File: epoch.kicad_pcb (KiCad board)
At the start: 4 copper layers, 28 x 34 mm, 29 parts, among them J1 USB_OTG, J2 CONN_01X05, P3 CONN_01X10, SW1 SW_Reset, SW2 SW_Up, SW3 SW_Middle, SW4 SW_Down, U1 MIC5219-3.3BM5, U2 ATSAMD21Ennc-AU, U3 DS3231MZ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

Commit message: Add back corner drill holes
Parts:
- added REF**: 1pin, Connectors:1pin_nosilk, F.Cu at (103.3, 56.5)
- added REF**: 1pin, Connectors:1pin_nosilk, F.Cu at (127.3, 56.5)
- added REF**: 1pin, Connectors:1pin_nosilk, F.Cu at (103.4, 86.4)
- added REF**: 1pin, Connectors:1pin_nosilk, F.Cu at (127.3, 86.4)
- renumbered D1 to LED
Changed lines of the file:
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@@
     (links 80)
     (no_connects 0)
-    (area 101.218844 54.355999 129.463801 88.620601)
+    (area 82.8926 44.9831 152.154639 97.2934)
     (thickness 1.6002)
     (drawings 20)
@@
     (1 In1.Cu signal)
     (2 In2.Cu signal)
-    (31 B.Cu signal hide)
+    (31 B.Cu signal)
     (34 B.Paste user)
     (35 F.Paste user)
@@
   )
   (setup
-    (last_trace_width 0.3)
+    (last_trace_width 0.1524)
     (user_trace_width 0.1524)
     (user_trace_width 0.2)
@@
       (effects (font (size 1 1) (thickness 0.15)))
     )
-    (fp_text user %R (at -4.1275 -13.1445 180) (layer F.Fab)
+    (fp_text user %R (at -18.3515 -15.24 180) (layer F.Fab)
       (effects (font (size 1 1) (thickness 0.15)))
     )
@@
       (net 2 "(GND)"))
   )
+  (module Connectors:1pin_nosilk (layer F.Cu)
+    (at 103.3272 56.4642)
+    (descr "module 1 pin (ou trou mecanique de percage)")
+    (tags DEV)
+    (fp_text reference REF** (at -9.271 -3.302) (layer F.SilkS)
+      (effects (font (size 1 1) (thickness 0.15)))
+    )
+    (fp_text value 1pin (at -8.5725 -0.381) (layer F.Fab) hide
+      (effects (font (size 1 1) (thickness 0.15)))
+    )
+    (fp_circle (center 0 0) (end 2 0.8) (layer F.Fab) (width 0.1))
+    (fp_circle (center 0 0) (end 2.6 0) (layer F.CrtYd) (width 0.05))
+    (pad "" np_thru_hole circle (at 0 0) (size 2.2 2.2) (drill 2.2) (layers *.Cu *.Mask))
+  )
+  (module Connectors:1pin_nosilk (layer F.Cu)
+    (at 127.3048 56.5404)
+    (descr "module 1 pin (ou trou mecanique de percage)")
+    (tags DEV)
+    (fp_text reference REF** (at 1.2192 -13.2334) (layer F.SilkS)
+      (effects (font (size 1 1) (thickness 0.15)))
+    )
+    (fp_text value 1pin (at -20.7518 -11.2014) (layer F.Fab) hide
+      (effects (font (size 1 1) (thickness 0.15)))
+    )
+    (fp_circle (center 0 0) (end 2 0.8) (layer F.Fab) (width 0.1))
+    (fp_circle (center 0 0) (end 2.6 0) (layer F.CrtYd) (width 0.05))
+    (pad "" np_thru_hole circle (at 0 0) (size 2.2 2.2) (drill 2.2) (layers *.Cu *.Mask))
+  )
+  (module Connectors:1pin_nosilk (layer F.Cu)
+    (at 103.4288 86.4108)
+    (descr "module 1 pin (ou trou mecanique de percage)")
+    (tags DEV)
+    (fp_text reference REF** (at -9.271 -3.302) (layer F.SilkS)
+      (effects (font (size 1 1) (thickness 0.15)))
+    )
+    (fp_text value 1pin (at -8.5725 -0.381) (layer F.Fab) hide
+      (effects (font (size 1 1) (thickness 0.15)))
+    )
+    (fp_circle (center 0 0) (end 2 0.8) (layer F.Fab) (width 0.1))
+    (fp_circle (center 0 0) (end 2.6 0) (layer F.CrtYd) (width 0.05))
+    (pad "" np_thru_hole circle (at 0 0) (size 2.2 2.2) (drill 2.2) (layers *.Cu *.Mask))
+  )
+  (module Connectors:1pin_nosilk (layer F.Cu)
+    (at 127.2794 86.4108)
+    (descr "module 1 pin (ou trou mecanique de percage)")
+    (tags DEV)
+    (fp_text reference REF** (at -9.271 -3.302) (layer F.SilkS)
+      (effects (font (size 1 1) (thickness 0.15)))
+    )
+    (fp_text value 1pin (at 19.4056 1.8542) (layer F.Fab) hide
+      (effects (font (size 1 1) (thickness 0.15)))
+    )
+    (fp_circle (center 0 0) (end 2 0.8) (layer F.Fab) (width 0.1))
+    (fp_circle (center 0 0) (end 2.6 0) (layer F.CrtYd) (width 0.05))
+    (pad "" np_thru_hole circle (at 0 0) (size 2.2 2.2) (drill 2.2) (layers *.Cu *.Mask))
+  )
   (module Buttons_Switches_SMD:SW_SPST_B3U-3000P (layer B.Cu)
     (at 102.616 61.468 270)
@@
     (tags "LED led 0805 SMD smd SMT smt smdled SMDLED smtled SMTLED")
     (attr smd)
-    (fp_text reference D1 (at 0 -1.45 90) (layer F.SilkS)
-      (effects (font (size 1 1) (thickness 0.15)))
-    )
-    (fp_text value LED (at -0.4318 9.3472 90) (layer F.Fab)
+    (fp_text reference LED (at -0.7112 -1.524 90) (layer F.SilkS)
+      (effects (font (size 1 1) (thickness 0.15)))
+    )
+    (fp_text value LED (at -0.8382 11.303 90) (layer F.Fab)
       (effects (font (size 1 1) (thickness 0.15)))
     )
@@
   (gr_line (start 111.0615 88.483) (end 111.887 87.63) (angle 90) (layer Edge.Cuts) (width 0.254))
   (gr_line (start 103.4034 88.4936) (end 111.0488 88.4936) (angle 90) (layer Edge.Cuts) (width 0.254))
-  (gr_text 3.3V (at 126.492 86.614) (layer F.SilkS)
+  (gr_text 3.3V (at 121.158 86.741) (layer F.SilkS)
     (effects (font (size 0.6 0.6) (thickness 0.125)))
   )
-  (gr_text SDIO (at 126.365 85.344) (layer F.SilkS)
+  (gr_text SDIO (at 121.285 85.471) (layer F.SilkS)
     (effects (font (size 0.6 0.6) (thickness 0.125)))
   )

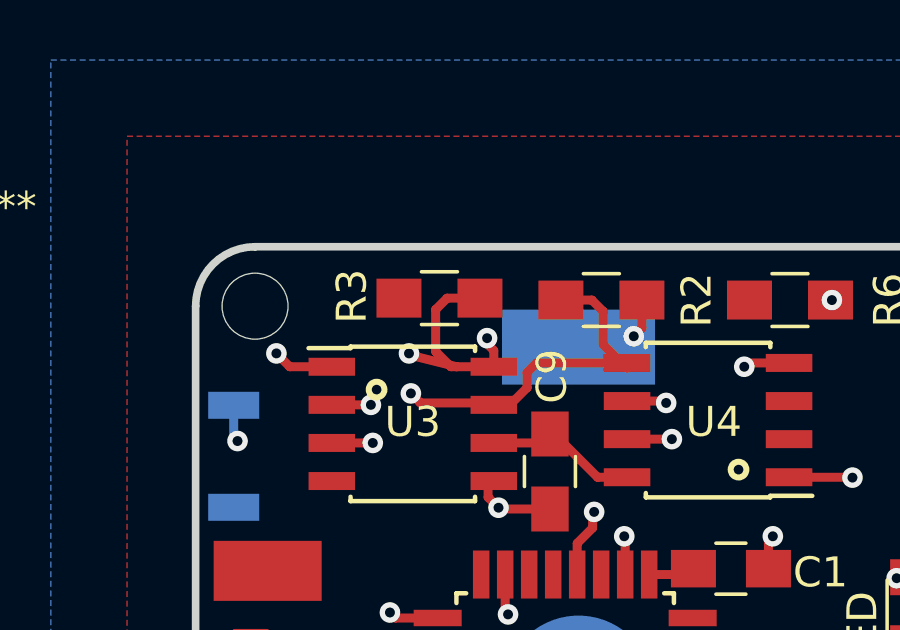
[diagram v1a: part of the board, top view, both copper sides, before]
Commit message: correct the routing after adding drills back
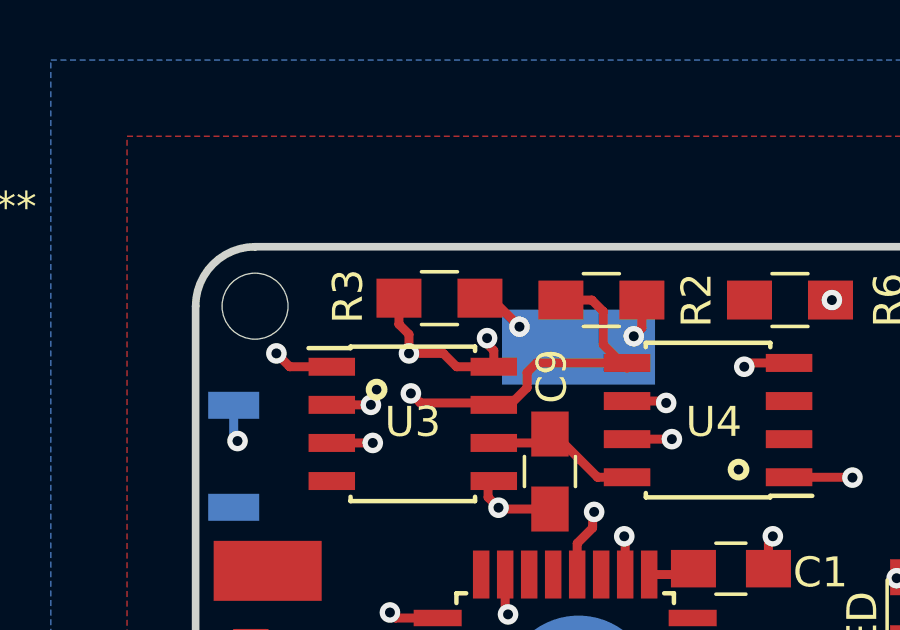
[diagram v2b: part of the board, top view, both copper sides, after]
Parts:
- turned R3 to 180 degrees
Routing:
- net (+3.3): track 21.1 -> 25.1 mm, vias 2 -> 3
- net SCL: track 34.0 -> 32.3 mm
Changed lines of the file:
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@@
     (links 80)
     (no_connects 0)
-    (area 82.8926 44.9831 152.154639 97.2934)
+    (area 82.8926 42.3796 152.154639 97.2934)
     (thickness 1.6002)
     (drawings 20)
-    (tracks 416)
+    (tracks 420)
     (zones 0)
-    (modules 29)
+    (modules 33)
     (nets 43)
   )
@@
   )
   (setup
-    (last_trace_width 0.1524)
+    (last_trace_width 0.3)
     (user_trace_width 0.1524)
     (user_trace_width 0.2)
@@
   )
   (module Resistors_SMD:R_0805_HandSoldering (layer F.Cu)
-    (at 109.474 56.1975)
+    (at 109.474 56.1975 180)
     (descr "Resistor SMD 0805, hand soldering")
     (tags "resistor 0805")
     (attr smd)
-    (fp_text reference R3 (at -2.921 -0.0635 270) (layer F.SilkS)
-      (effects (font (size 1 1) (thickness 0.15)))
-    )
-    (fp_text value 4.7K (at -16.002 17.018) (layer F.Fab)
-      (effects (font (size 1 1) (thickness 0.15)))
-    )
-    (fp_text user %R (at -15.494 4.2545) (layer F.Fab)
+    (fp_text reference R3 (at 3.048 0.0635 450) (layer F.SilkS)
+      (effects (font (size 1 1) (thickness 0.15)))
+    )
+    (fp_text value 4.7K (at -16.002 17.018 180) (layer F.Fab)
+      (effects (font (size 1 1) (thickness 0.15)))
+    )
+    (fp_text user %R (at -0.127 9.2075 180) (layer F.Fab)
       (effects (font (size 1 1) (thickness 0.15)))
     )
@@
     (fp_line (start 2.35 0.9) (end 2.35 -0.9) (layer F.CrtYd) (width 0.05))
     (fp_line (start 2.35 0.9) (end -2.35 0.9) (layer F.CrtYd) (width 0.05))
-    (pad 1 smd rect (at -1.35 0) (size 1.5 1.3) (layers F.Cu F.Paste F.Mask)
-      (net 1 "(+3.3)"))
-    (pad 2 smd rect (at 1.35 0) (size 1.5 1.3) (layers F.Cu F.Paste F.Mask)
+    (pad 1 smd rect (at -1.35 0 180) (size 1.5 1.3) (layers F.Cu F.Paste F.Mask)
+      (net 1 "(+3.3)"))
+    (pad 2 smd rect (at 1.35 0 180) (size 1.5 1.3) (layers F.Cu F.Paste F.Mask)
       (net 19 SCL))
     (model Resistors_SMD.3dshapes/R_0805.wrl
@@
   (gr_line (start 103.3272 54.483) (end 127.3556 54.483) (angle 90) (layer Edge.Cuts) (width 0.254))
   (gr_line (start 129.33426 86.44382) (end 129.3368 56.4642) (angle 90) (layer Edge.Cuts) (width 0.254))
+  (segment (start 110.824 56.1975) (end 111.1885 56.1975) (width 0.3) (layer F.Cu) (net 1))
+  (segment (start 111.1885 56.1975) (end 112.141 57.15) (width 0.3) (layer F.Cu) (net 1))
+  (segment (start 112.141 57.15) (end 112.8195 57.8285) (width 0.3) (layer B.Cu) (net 1))
+  (via (at 112.141 57.15) (size 0.6858) (drill 0.3302) (layers F.Cu B.Cu) (net 1))
+  (segment (start 112.8195 57.8285) (end 114.1095 57.8285) (width 0.3) (layer B.Cu) (net 1))
   (segment (start 115.55 81.923) (end 115.55 82.951) (width 0.3) (layer F.Cu) (net 1))
   (segment (start 115.55 82.951) (end 115.189 83.312) (width 0.3) (layer F.Cu) (net 1))
@@
   (segment (start 114.935 56.642) (end 114.554 56.261) (width 0.3) (layer F.Cu) (net 18))
   (segment (start 114.554 56.261) (end 113.5215 56.261) (width 0.3) (layer F.Cu) (net 18))
+  (segment (start 108.458 58.039) (end 109.601 58.039) (width 0.3) (layer F.Cu) (net 19))
+  (segment (start 110.0455 58.4835) (end 111.0945 58.4835) (width 0.3) (layer F.Cu) (net 19))
+  (segment (start 109.601 58.039) (end 110.0455 58.4835) (width 0.3) (layer F.Cu) (net 19))
+  (segment (start 108.124 56.1975) (end 108.124 57.07) (width 0.3) (layer F.Cu) (net 19))
+  (segment (start 108.458 57.404) (end 108.458 58.039) (width 0.3) (layer F.Cu) (net 19))
+  (segment (start 108.124 57.07) (end 108.458 57.404) (width 0.3) (layer F.Cu) (net 19))
   (segment (start 108.0135 67.691) (end 104.521 67.691) (width 0.3) (layer In1.Cu) (net 19))
-  (segment (start 110.0455 58.4835) (end 108.5215 58.1025) (width 0.3) (layer F.Cu) (net 19))
   (segment (start 108.458 58.039) (end 108.5215 58.1025) (width 0.3) (layer F.Cu) (net 19))
   (via (at 108.458 58.039) (size 0.6858) (drill 0.3302) (layers F.Cu B.Cu) (net 19))
@@
   (segment (start 111.0615 57.719) (end 111.0615 57.531) (width 0.3) (layer F.Cu) (net 19))
   (segment (start 111.285 57.9425) (end 111.0615 57.719) (width 0.3) (layer F.Cu) (net 19))
-  (segment (start 111.0945 58.4835) (end 110.0455 58.4835) (width 0.3) (layer F.Cu) (net 19))
-  (segment (start 110.0455 58.4835) (end 109.855 58.4835) (width 0.3) (layer F.Cu) (net 19))
-  (segment (start 109.855 58.4835) (end 109.347 57.9755) (width 0.3) (layer F.Cu) (net 19))
-  (segment (start 109.347 57.9755) (end 109.347 56.5785) (width 0.3) (layer F.Cu) (net 19))
-  (segment (start 109.347 56.5785) (end 109.728 56.1975) (width 0.3) (layer F.Cu) (net 19))
-  (segment (start 109.728 56.1975) (end 110.824 56.1975) (width 0.3) (layer F.Cu) (net 19))
   (segment (start 115.7275 60.8965) (end 117.221 60.8965) (width 0.3) (layer F.Cu) (net 20))
   (via (at 117.221 60.8965) (size 0.6858) (drill 0.3302) (layers F.Cu B.Cu) (net 20))

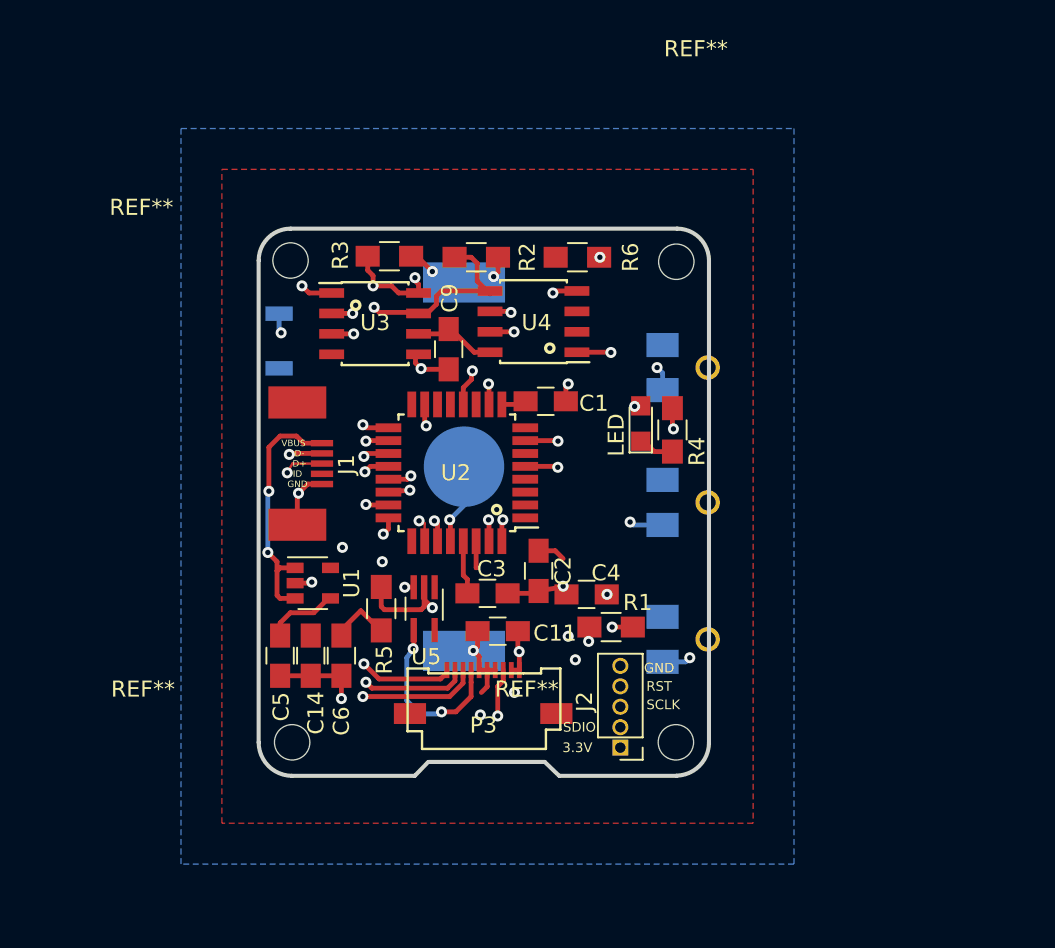
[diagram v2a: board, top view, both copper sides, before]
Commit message: Update drills
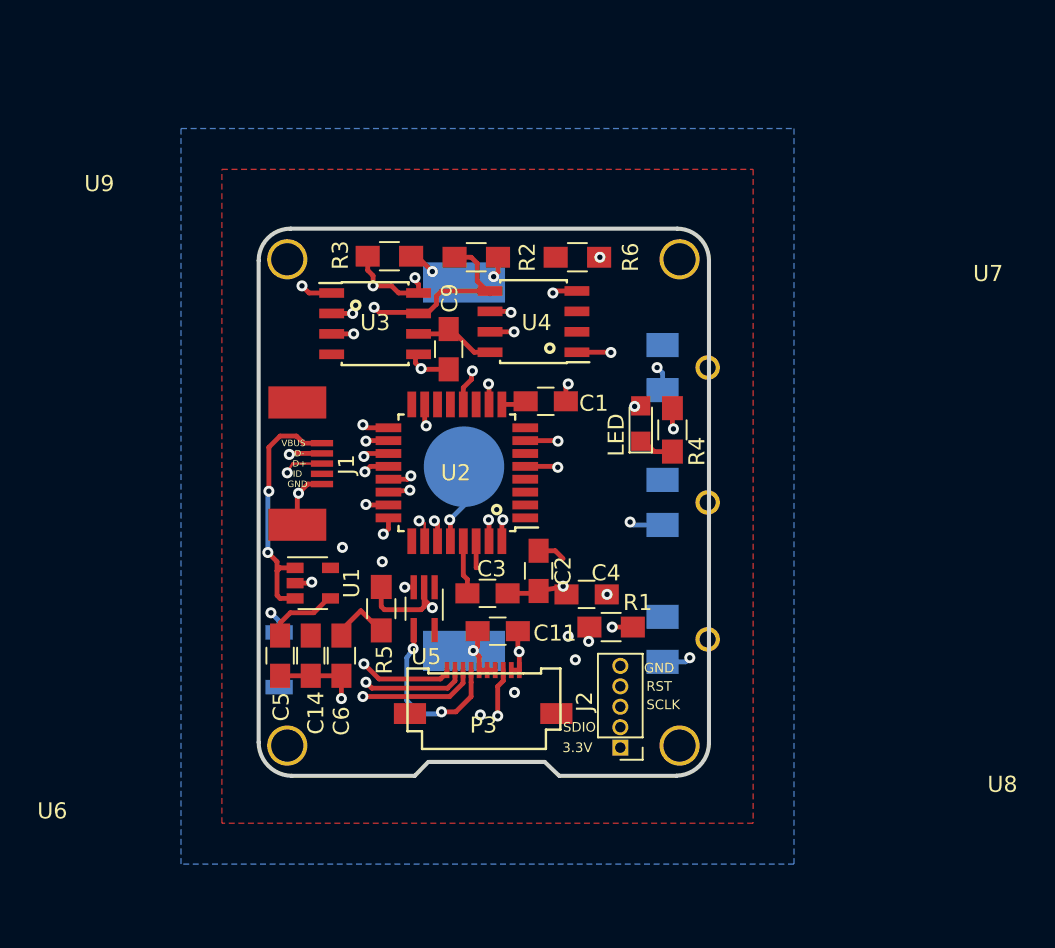
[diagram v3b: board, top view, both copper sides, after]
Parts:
- removed REF** (x4): 1pin, Connectors:1pin_nosilk
- added U6: MH2mm, my-fp-library:MH2mm, F.Cu at (103.1, 86.6)
- added U7: MH2mm, my-fp-library:MH2mm, F.Cu at (127.4, 56.4)
- added U8: MH2mm, my-fp-library:MH2mm, F.Cu at (127.5, 86.7)
- added U9: MH2mm, my-fp-library:MH2mm, F.Cu at (103.3, 56.1)
- moved SW1 19.8 mm to (102.6, 81.3)
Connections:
- J1 pad 4: Net-(J1-Pad4) -> (no net)
- U2 pad 1: Net-(U2-Pad1) -> (no net)
- U2 pad 11: Net-(U2-Pad11) -> (no net)
- U2 pad 13: Net-(U2-Pad13) -> (no net)
- U2 pad 14: Net-(U2-Pad14) -> (no net)
- U2 pad 16: Net-(U2-Pad16) -> (no net)
- U2 pad 2: Net-(U2-Pad2) -> (no net)
- U2 pad 25: Net-(U2-Pad25) -> (no net)
- U2 pad 3: Net-(U2-Pad3) -> (no net)
- U2 pad 4: Net-(U2-Pad4) -> (no net)
- U2 pad 6: Net-(U2-Pad6) -> (no net)
- U2 pad 8: Net-(U2-Pad8) -> (no net)
- U3 pad 4: Net-(U3-Pad4) -> (no net)
- U4 pad 2: Net-(U4-Pad2) -> (no net)
- U4 pad 3: Net-(U4-Pad3) -> (no net)
- U5 pad 1: Net-(U5-Pad1) -> (no net)
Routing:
- net Net-(R1-Pad1): track 40.2 -> 26.6 mm
- net (+3.3): track 25.1 -> 23.5 mm

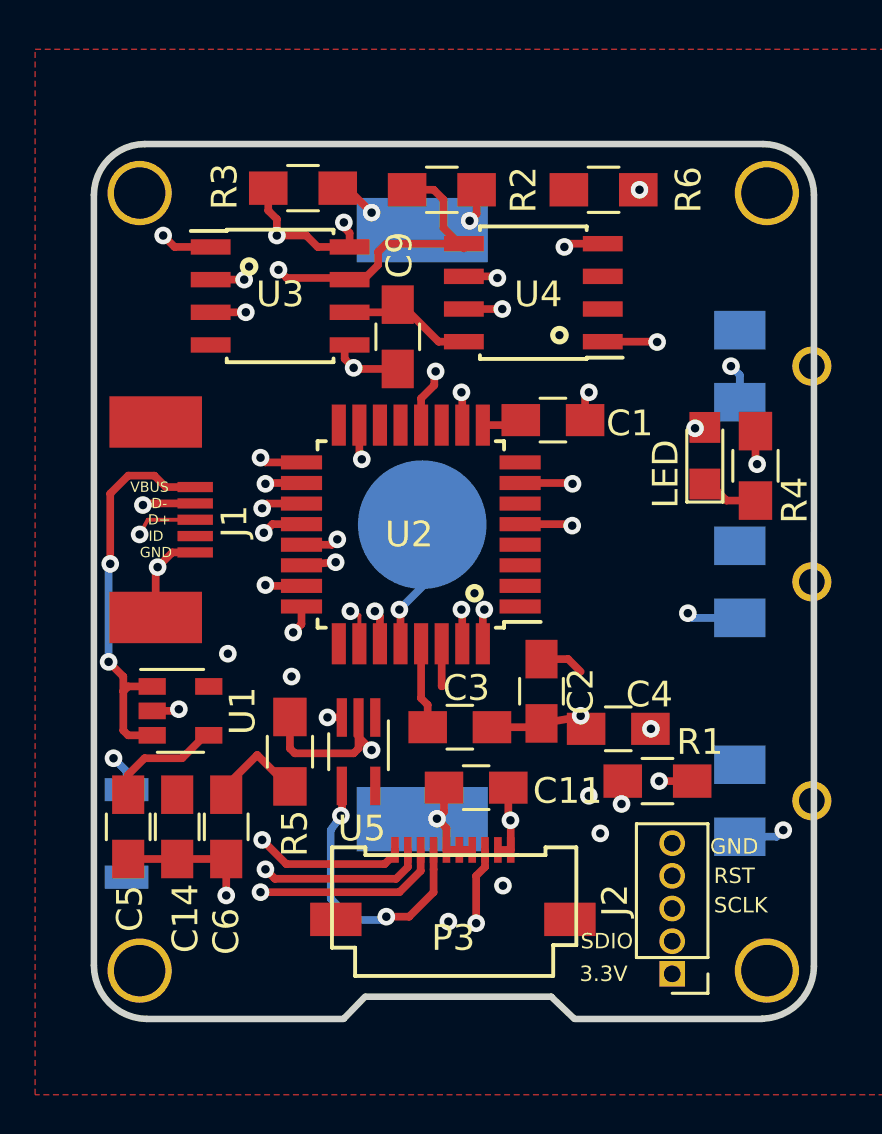
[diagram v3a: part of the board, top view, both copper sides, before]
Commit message: Use same connector for hotswap
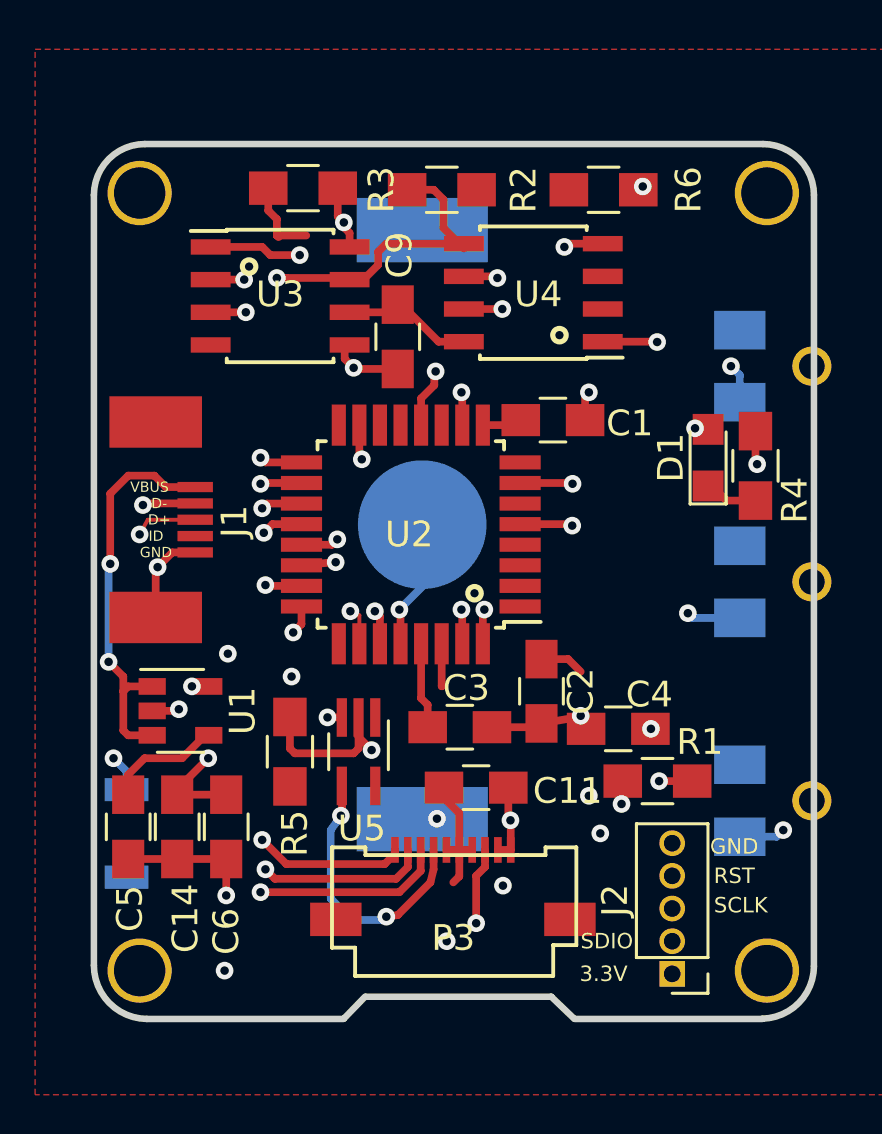
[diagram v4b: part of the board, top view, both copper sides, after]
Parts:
- removed LED: LED, LEDs:LED_0805
- added D1: LED, LEDs:LED_0805, F.Cu at (125.2, 66.7)
- turned R3 to 0 degrees
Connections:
- BT1 pad 1: (+3.3) -> SWDCLK/+3.3V(BATT)
- C14 pad 1: (+3.3) -> SWDIO/+3.3V(REGUL)
- C6 pad 1: (+3.3) -> SWDIO/+3.3V(REGUL)
- J2 pad 2: SWDIO -> SWDIO/+3.3V(REGUL)
- J2 pad 3: SWDCLK -> SWDCLK/+3.3V(BATT)
- U1 pad 5: (+3.3) -> SWDIO/+3.3V(REGUL)
- U2 pad 31: SWDCLK -> SWDCLK/+3.3V(BATT)
- U2 pad 32: SWDIO -> SWDIO/+3.3V(REGUL)
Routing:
- net SWDIO/+3.3V(REGUL): track 0.00 -> 50.4 mm, vias 0 -> 5
- net SWDCLK/+3.3V(BATT): track 0.00 -> 26.8 mm, vias 0 -> 2
- net SWDIO: track 21.0 -> 0.00 mm, vias 2 -> 0
- net SWDCLK: track 20.4 -> 0.00 mm, vias 1 -> 0
- net 32KHz: track 32.0 -> 44.6 mm
- net (+3.3): track 23.5 -> 18.4 mm, vias 3 -> 0
- net RESET: track 44.4 -> 46.0 mm
- net SCL: track 32.3 -> 31.5 mm, vias 4 -> 3
